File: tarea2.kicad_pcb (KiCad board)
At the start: 2 copper layers, 13 parts, among them IC1 LDO40LPURY, J1 Conn_01x02_Pin, J2 Conn_01x06_Pin, U1 STM32G030K8Tx

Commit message: Colocación inicial de los elementos en la PCB
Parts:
- moved J2 32.3 mm to (146.9, 123.8), turned to 180 degrees
- moved C4(des)2 23.8 mm to (139.3, 104.5), turned to 90 degrees
- moved C4(des)3 23.8 mm to (147.8, 104.5)
- moved IC1 23.8 mm to (143.7, 104.5)
- moved C4(des)1 19.7 mm to (163.0, 111.7)
- moved R1 16.9 mm to (152.0, 116.6), turned to 180 degrees
- moved J1 16.5 mm to (156.0, 104.4), turned to 90 degrees
- moved C1 15.7 mm to (152.0, 119.1), turned to 180 degrees
- moved U1 15.3 mm to (161.5, 119.1), turned to -90 degrees
- moved R2 10.3 mm to (155.6, 112.1), turned to 180 degrees
- moved R3 5.59 mm to (159.9, 112.1)
- moved C3 4.54 mm to (160.0, 108.6), turned to 0 degrees
- moved C2 3.47 mm to (155.6, 108.6), turned to 180 degrees
- renumbered C4(desacople)1 to C4(des)1, C4(desacople)2 to C4(des)2, C4(desacople)3 to C4(des)3
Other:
- board outline added: 37 x 30.5 mm

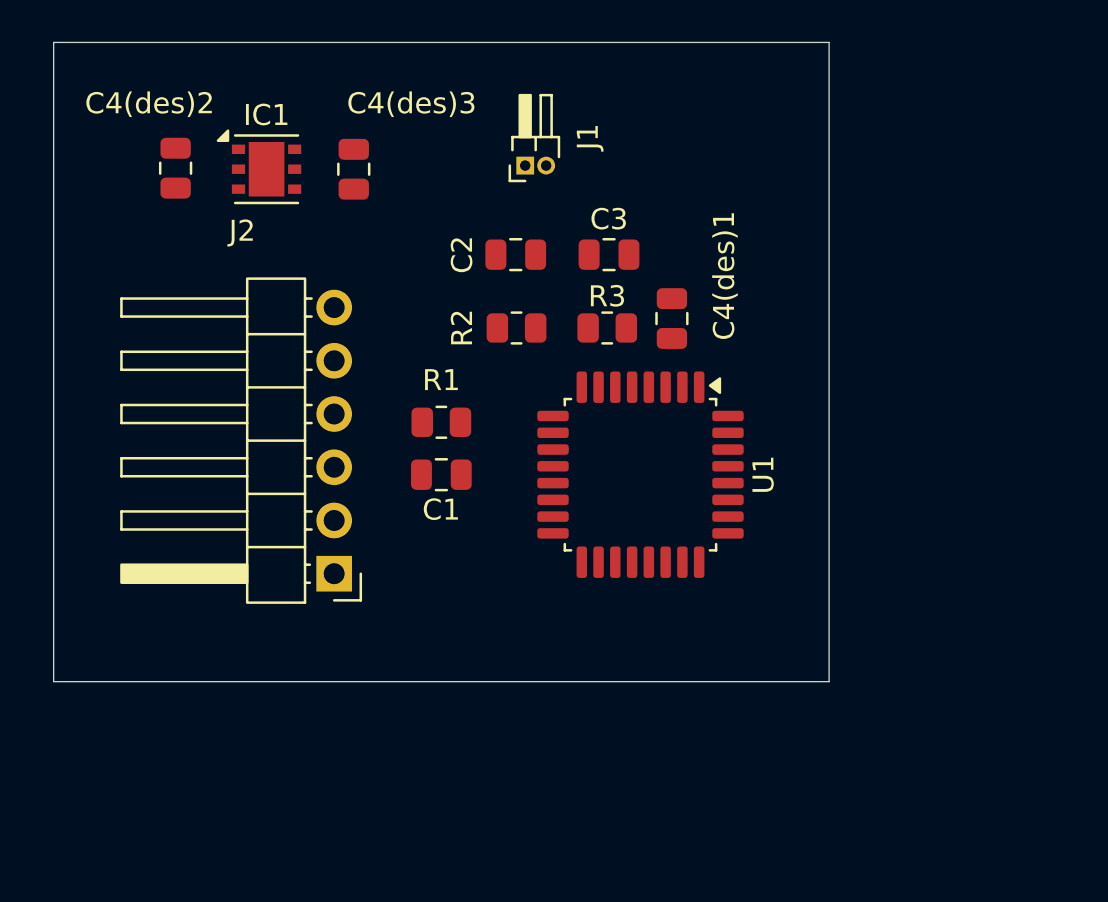
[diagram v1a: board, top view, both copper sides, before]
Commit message: He enrutado los componentes, creando una capa inferior de masa común con vías que facilita el enrutado. He rebajado el margen de holgura a 0,15mm y el DRC está limpio de errores.
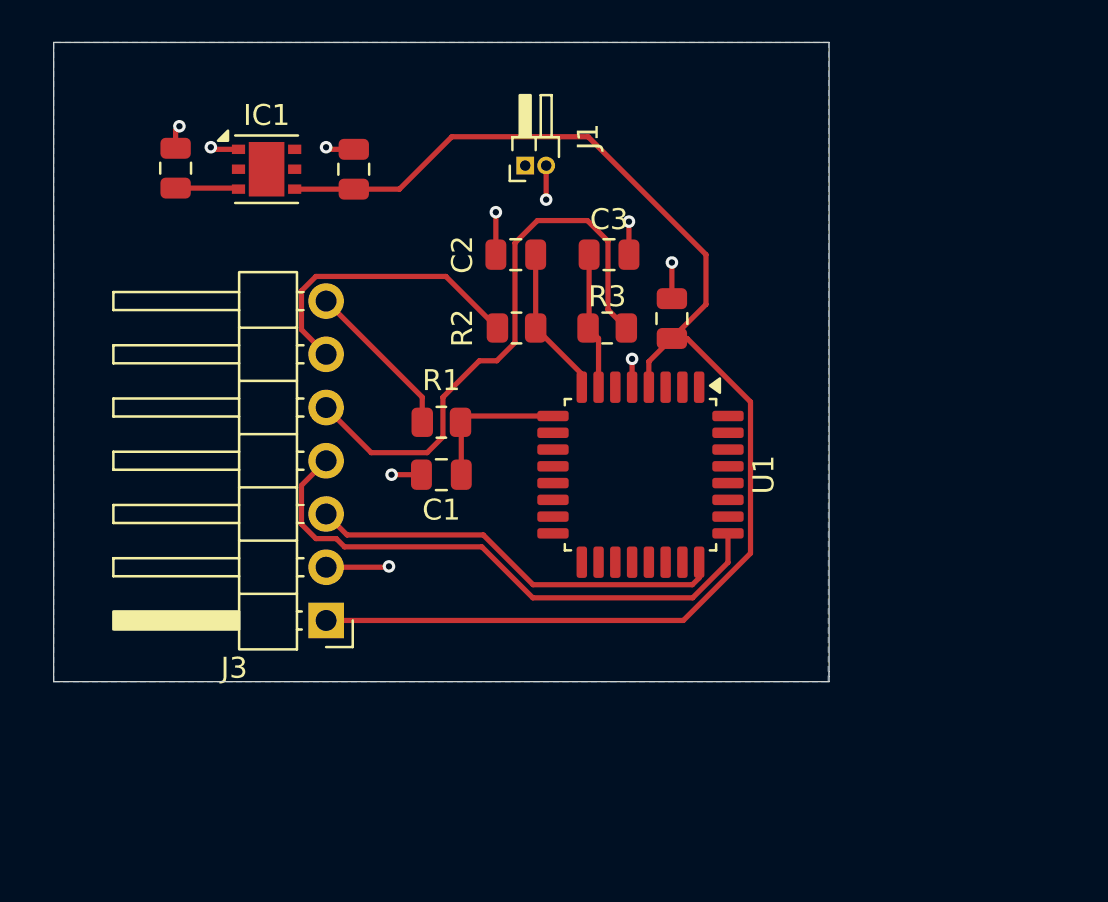
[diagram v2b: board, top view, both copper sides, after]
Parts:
- removed J2: Conn_01x06_Pin, Connector_PinHeader_2.54mm:PinHeader_1x06_P2.54mm_Horizontal
- added J3: Conn_01x07, Connector_PinHeader_2.54mm:PinHeader_1x07_P2.54mm_Horizontal, F.Cu at (146.5, 126.1)
- renumbered C4(des)1 to C4(desacople)1, C4(des)2 to C4(desacople)2, C4(des)3 to C4(desacople)3
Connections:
- C4(desacople)2 pad 2: Net-(IC1-GND_1) -> /Alimentación/GND
- C4(desacople)3 pad 2: Net-(IC1-GND_1) -> /Alimentación/GND
- IC1 pad 1: Net-(IC1-GND_1) -> /Alimentación/GND
- R1 pad 2: unconnected-(R1-Pad2) -> Net-(J3-Pin_7)
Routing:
- net /Alimentación/VDD: track 0.00 -> 64.3 mm
- net Net-(J3-Pin_5): track 0.00 -> 27.7 mm
- net Net-(J3-Pin_4): track 0.00 -> 27.4 mm
- net Net-(J3-Pin_3): track 0.00 -> 20.1 mm
- net /Alimentación/GND: track 0.00 -> 17.2 mm, vias 0 -> 10
- net Net-(J3-Pin_6): track 0.00 -> 14.2 mm
- net Net-(J3-Pin_7): track 0.00 -> 7.69 mm
- net Net-(U1-PA1): track 0.00 -> 7.24 mm
- net Net-(U1-PA2): track 0.00 -> 7.05 mm
- net Net-(U1-PA0): track 0.00 -> 6.55 mm
- net Net-(IC1-VIN): track 0.00 -> 3.02 mm
- added copper zone on B.Cu, net /Alimentación/GND

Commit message: elimada una vía innecesaria
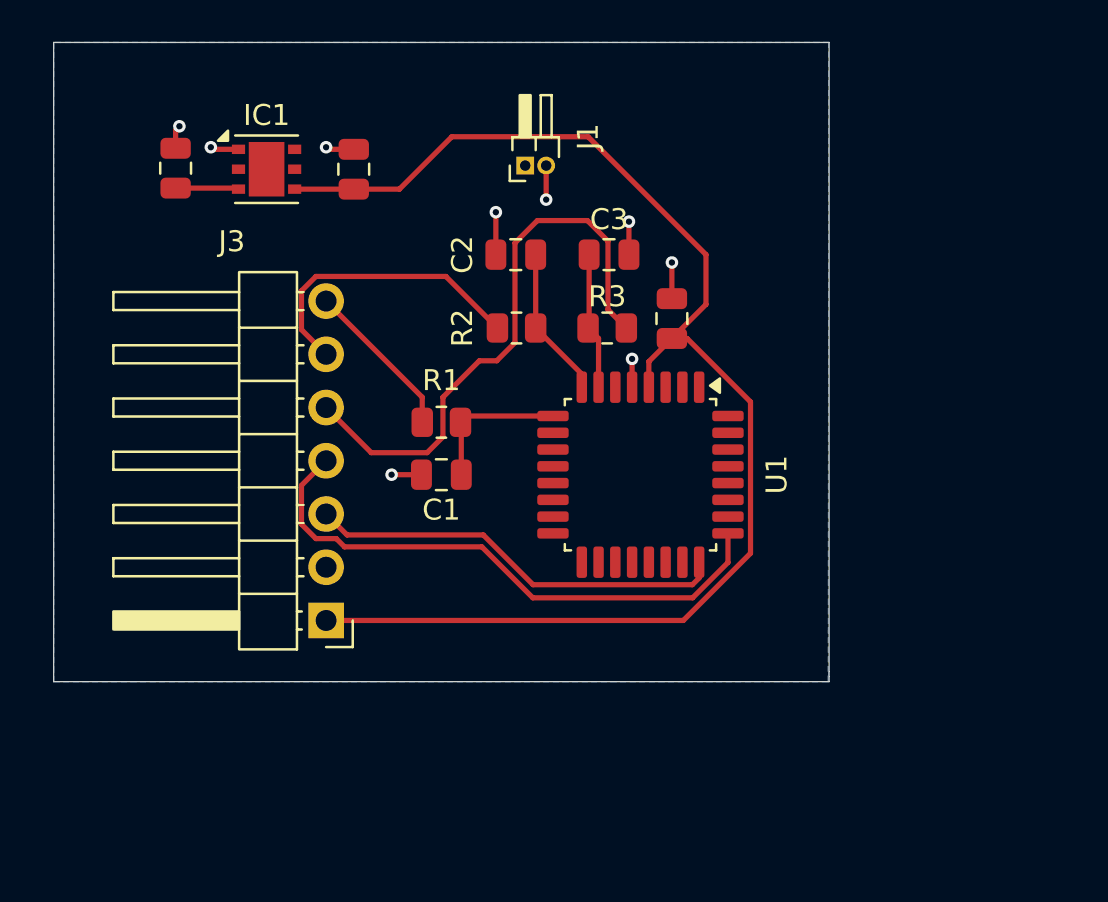
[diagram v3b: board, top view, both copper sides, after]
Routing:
- net /Alimentación/GND: track 17.2 -> 14.2 mm, vias 10 -> 9
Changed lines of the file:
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@@
 		(tags "LQFP QFP")
 		(property "Reference" "U1"
-			(at 0 -5.88 90)
+			(at 0 -6.5 90)
 			(layer "F.SilkS")
 			(effects
@@
 			(layer "F.Fab")
 		)
-		(fp_text user "${REFERENCE}"
-			(at 0 0 90)
-			(layer "F.Fab")
-			(effects
-				(font
-					(size 0.5 0.5)
-					(thickness 0.08)
-				)
-			)
-		)
 		(pad "1" smd roundrect
 			(at -0.95 0 90)
@@
 			(layer "F.Fab")
 		)
-		(fp_text user "${REFERENCE}"
-			(at 0 0 90)
-			(layer "F.Fab")
-			(effects
-				(font
-					(size 0.5 0.5)
-					(thickness 0.08)
-				)
-			)
-		)
 		(pad "1" smd roundrect
 			(at -0.95 0 90)
@@
 		(tags "Through hole angled pin header THT 1x07 2.54mm single row")
 		(property "Reference" "J3"
-			(at 4.385 -2.27 0)
+			(at 4.5 18.08 0)
 			(layer "F.SilkS")
 			(effects
@@
 			(at 4.385 17.51 0)
 			(layer "F.Fab")
+			(hide yes)
 			(effects
 				(font
@@
 			(at 0.425 3.866 0)
 			(layer "F.Fab")
+			(hide yes)
 			(effects
 				(font
@@
 			(layer "F.Fab")
 		)
-		(fp_text user "${REFERENCE}"
-			(at 0 0 90)
-			(layer "F.Fab")
-			(effects
-				(font
-					(size 0.5 0.5)
-					(thickness 0.08)
-				)
-			)
-		)
 		(pad "1" smd roundrect
 			(at -0.95 0 90)
@@
 	)
 	(segment
+		(start 146.013299 109.665)
+		(end 152.215 109.665)
+		(width 0.25)
+		(layer "F.Cu")
+		(net "Net-(J3-Pin_6)")
+	)
+	(segment
+		(start 146.5 113.38)
+		(end 145.325 112.205)
+		(width 0.25)
+		(layer "F.Cu")
+		(net "Net-(J3-Pin_6)")
+	)
+	(segment
+		(start 152.215 109.665)
+		(end 154.675 112.125)
+		(width 0.25)
+		(layer "F.Cu")
+		(net "Net-(J3-Pin_6)")
+	)
+	(segment
+		(start 145.325 112.205)
+		(end 145.325 110.353299)
+		(width 0.25)
+		(layer "F.Cu")
+		(net "Net-(J3-Pin_6)")
+	)
+	(segment
+		(start 145.325 110.353299)
+		(end 146.013299 109.665)
+		(width 0.25)
+		(layer "F.Cu")
+		(net "Net-(J3-Pin_6)")
+	)
+	(segment
 		(start 152.5 103)
 		(end 150 105.5)
@@
 	)
 	(segment
-		(start 146.5 123.54)
-		(end 149.46 123.54)
-		(width 0.25)
-		(layer "F.Cu")
-		(net "/Alimentación/GND")
-	)
-	(segment
 		(start 163 110.725)
 		(end 163 109)
@@
 	)
 	(segment
-		(start 149.46 123.54)
-		(end 149.5 123.5)
-		(width 0.25)
-		(layer "F.Cu")
-		(net "/Alimentación/GND")
-	)
-	(segment
 		(start 139.32 102.68)
 		(end 139.5 102.5)
@@
 	)
 	(via
-		(at 149.5 123.5)
-		(size 0.6)
-		(drill 0.3)
-		(layers "F.Cu" "B.Cu")
-		(net "/Alimentación/GND")
-	)
-	(via
 		(at 154.6 106.6)
 		(size 0.6)
@@
 	)
 	(segment
-		(start 139.32 105.45)
-		(end 142.27 105.45)
-		(width 0.25)
-		(layer "F.Cu")
-		(net "Net-(IC1-VIN)")
-	)
-	(segment
-		(start 142.27 105.45)
-		(end 142.32 105.5)
-		(width 0.25)
-		(layer "F.Cu")
-		(net "Net-(IC1-VIN)")
-	)
-	(segment
 		(start 156.375 124.375)
 		(end 154 122)
@@
 	)
 	(segment
-		(start 155.5125 108.0674)
-		(end 156.5799 107)
+		(start 146.5 118.46)
+		(end 145.325 119.635)
 		(width 0.25)
 		(layer "F.Cu")
-		(net "Net-(J3-Pin_5)")
+		(net "Net-(J3-Pin_4)")
 	)
 	(segment
-		(start 156.5799 107)
-		(end 158.9701 107)
+		(start 146.986701 122.175)
+		(end 147.379899 122.568198)
 		(width 0.25)
 		(layer "F.Cu")
-		(net "Net-(J3-Pin_5)")
+		(net "Net-(J3-Pin_4)")
 	)
 	(segment
-		(start 158.9701 107)
-		(end 159.95 107.9799)
+		(start 165.675 123.31486)
+		(end 165.675 121.925)
 		(width 0.25)
 		(layer "F.Cu")
-		(net "Net-(J3-Pin_5)")
+		(net "Net-(J3-Pin_4)")
 	)
 	(segment
-		(start 146.5 115.92)
-		(end 148.655 118.075)
+		(start 145.325 121.486701)
+		(end 146.013299 122.175)
 		(width 0.25)
 		(layer "F.Cu")
-		(net "Net-(J3-Pin_5)")
+		(net "Net-(J3-Pin_4)")
 	)
 	(segment
-		(start 159.95 111.25)
-		(end 160.825 112.125)
+		(start 145.325 119.635)
+		(end 145.325 121.486701)
 		(width 0.25)
 		(layer "F.Cu")
-		(net "Net-(J3-Pin_5)")
+		(net "Net-(J3-Pin_4)")
 	)
 	(segment
-		(start 148.655 118.075)
-		(end 151.3201 118.075)
+		(start 156.363604 125)
+		(end 163.98986 125)
 		(width 0.25)
 		(layer "F.Cu")
-		(net "Net-(J3-Pin_5)")
+		(net "Net-(J3-Pin_4)")
 	)
 	(segment
-		(start 152.075 115.42745)
-		(end 153.81245 113.69)
+		(start 147.379899 122.568198)
+		(end 153.931802 122.568198)
 		(width 0.25)
 		(layer "F.Cu")
-		(net "Net-(J3-Pin_5)")
+		(net "Net-(J3-Pin_4)")
 	)
 	(segment
-		(start 151.3201 118.075)
-		(end 152.075 117.3201)
+		(start 146.013299 122.175)
+		(end 146.986701 122.175)
 		(width 0.25)
 		(layer "F.Cu")
-		(net "Net-(J3-Pin_5)")
+		(net "Net-(J3-Pin_4)")
 	)
 	(segment
-		(start 153.81245 113.69)
-		(end 154.6426 113.69)
+		(start 153.931802 122.568198)
+		(end 156.363604 125)
 		(width 0.25)
 		(layer "F.Cu")
-		(net "Net-(J3-Pin_5)")
+		(net "Net-(J3-Pin_4)")
 	)
 	(segment
-		(start 159.95 107.9799)
-		(end 159.95 111.25)
+		(start 163.98986 125)
+		(end 165.675 123.31486)
 		(width 0.25)
 		(layer "F.Cu")
-		(net "Net-(J3-Pin_5)")
+		(net "Net-(J3-Pin_4)")
 	)
 	(segment
-		(start 152.075 117.3201)
-		(end 152.075 115.42745)
+		(start 139.32 105.45)
+		(end 142.27 105.45)
 		(width 0.25)
 		(layer "F.Cu")
-		(net "Net-(J3-Pin_5)")
+		(net "Net-(IC1-VIN)")
 	)
 	(segment
-		(start 155.5125 112.8201)
-		(end 155.5125 108.0674)
+		(start 142.27 105.45)
+		(end 142.32 105.5)
 		(width 0.25)
 		(layer "F.Cu")
-		(net "Net-(J3-Pin_5)")
+		(net "Net-(IC1-VIN)")
 	)
 	(segment
-		(start 154.6426 113.69)
-		(end 155.5125 112.8201)
+		(start 155.5125 108.0674)
+		(end 156.5799 107)
 		(width 0.25)
 		(layer "F.Cu")
@@
 	)
 	(segment
-		(start 151.0875 115.4275)
-		(end 151.0875 116.625)
-		(width 0.25)
-		(layer "F.Cu")
-		(net "Net-(J3-Pin_7)")
-	)
-	(segment
-		(start 146.5 110.84)
-		(end 151.0875 115.4275)
-		(width 0.25)
-		(layer "F.Cu")
-		(net "Net-(J3-Pin_7)")
-	)
-	(segment
-		(start 146.5 118.46)
-		(end 145.325 119.635)
-		(width 0.25)
-		(layer "F.Cu")
-		(net "Net-(J3-Pin_4)")
-	)
-	(segment
-		(start 146.986701 122.175)
-		(end 147.379899 122.568198)
+		(start 156.5799 107)
+		(end 158.9701 107)
 		(width 0.25)
 		(layer "F.Cu")
-		(net "Net-(J3-Pin_4)")
+		(net "Net-(J3-Pin_5)")
 	)
 	(segment
-		(start 165.675 123.31486)
-		(end 165.675 121.925)
+		(start 158.9701 107)
+		(end 159.95 107.9799)
 		(width 0.25)
 		(layer "F.Cu")
-		(net "Net-(J3-Pin_4)")
+		(net "Net-(J3-Pin_5)")
 	)
 	(segment
-		(start 145.325 121.486701)
-		(end 146.013299 122.175)
+		(start 146.5 115.92)
+		(end 148.655 118.075)
 		(width 0.25)
 		(layer "F.Cu")
-		(net "Net-(J3-Pin_4)")
+		(net "Net-(J3-Pin_5)")
 	)
 	(segment
-		(start 145.325 119.635)
-		(end 145.325 121.486701)
+		(start 159.95 111.25)
+		(end 160.825 112.125)
 		(width 0.25)
 		(layer "F.Cu")
-		(net "Net-(J3-Pin_4)")
+		(net "Net-(J3-Pin_5)")
 	)
 	(segment
-		(start 156.363604 125)
-		(end 163.98986 125)
+		(start 148.655 118.075)
+		(end 151.3201 118.075)
 		(width 0.25)
 		(layer "F.Cu")
-		(net "Net-(J3-Pin_4)")
+		(net "Net-(J3-Pin_5)")
 	)
 	(segment
-		(start 147.379899 122.568198)
-		(end 153.931802 122.568198)
+		(start 152.075 115.42745)
+		(end 153.81245 113.69)
 		(width 0.25)
 		(layer "F.Cu")
-		(net "Net-(J3-Pin_4)")
+		(net "Net-(J3-Pin_5)")
 	)
 	(segment
-		(start 146.013299 122.175)
-		(end 146.986701 122.175)
+		(start 151.3201 118.075)
+		(end 152.075 117.3201)
 		(width 0.25)
 		(layer "F.Cu")
-		(net "Net-(J3-Pin_4)")
+		(net "Net-(J3-Pin_5)")
 	)
 	(segment
-		(start 153.931802 122.568198)
-		(end 156.363604 125)
+		(start 153.81245 113.69)
+		(end 154.6426 113.69)
 		(width 0.25)
 		(layer "F.Cu")
-		(net "Net-(J3-Pin_4)")
+		(net "Net-(J3-Pin_5)")
 	)
 	(segment
-		(start 163.98986 125)
-		(end 165.675 123.31486)
+		(start 159.95 107.9799)
+		(end 159.95 111.25)
 		(width 0.25)
 		(layer "F.Cu")
-		(net "Net-(J3-Pin_4)")
+		(net "Net-(J3-Pin_5)")
 	)
 	(segment
-		(start 146.013299 109.665)
-		(end 152.215 109.665)
+		(start 152.075 117.3201)
+		(end 152.075 115.42745)
 		(width 0.25)
 		(layer "F.Cu")
-		(net "Net-(J3-Pin_6)")
+		(net "Net-(J3-Pin_5)")
 	)
 	(segment
-		(start 146.5 113.38)
-		(end 145.325 112.205)
+		(start 155.5125 112.8201)
+		(end 155.5125 108.0674)
 		(width 0.25)
 		(layer "F.Cu")
-		(net "Net-(J3-Pin_6)")
+		(net "Net-(J3-Pin_5)")
 	)
 	(segment
-		(start 152.215 109.665)
-		(end 154.675 112.125)
+		(start 154.6426 113.69)
+		(end 155.5125 112.8201)
 		(width 0.25)
 		(layer "F.Cu")
-		(net "Net-(J3-Pin_6)")
+		(net "Net-(J3-Pin_5)")
 	)
 	(segment
-		(start 145.325 112.205)
-		(end 145.325 110.353299)
+		(start 151.0875 115.4275)
+		(end 151.0875 116.625)
 		(width 0.25)
 		(layer "F.Cu")
-		(net "Net-(J3-Pin_6)")
+		(net "Net-(J3-Pin_7)")
 	)
 	(segment
-		(start 145.325 110.353299)
-		(end 146.013299 109.665)
+		(start 146.5 110.84)
+		(end 151.0875 115.4275)
 		(width 0.25)
 		(layer "F.Cu")
-		(net "Net-(J3-Pin_6)")
+		(net "Net-(J3-Pin_7)")
 	)
 	(zone

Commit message: He completado la parte 1 de la práctica 4 y he subsanado los errores de la DRC
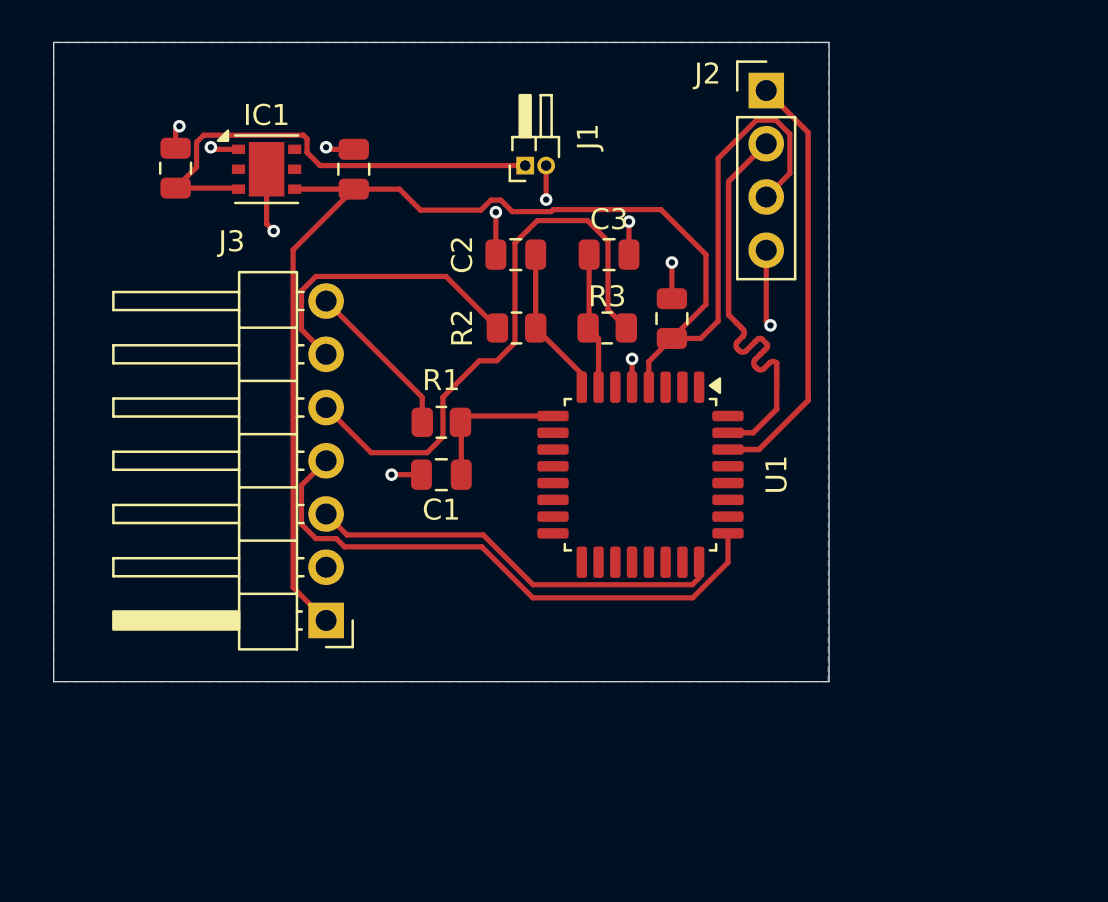
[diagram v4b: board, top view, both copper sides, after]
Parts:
- added J2: BUS I2C, Connector_PinHeader_2.54mm:PinHeader_1x04_P2.54mm_Vertical, F.Cu at (167.5, 100.8)
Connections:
- IC1 pad 7: Net-(IC1-GND_1) -> /Alimentación/GND
- J1 pad 1: unconnected-(J1-Pin_1-Pad1) -> Net-(IC1-VIN)
- U1 pad 30: unconnected-(U1-PB6-Pad30) -> Net-(J2-Pin_1)
- U1 pad 31: unconnected-(U1-PB7-Pad31) -> Net-(J2-Pin_2)
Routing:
- net Net-(J2-Pin_1): track 0.00 -> 20.4 mm
- net Net-(J2-Pin_2): track 0.00 -> 20.3 mm
- net Net-(IC1-VIN): track 3.02 -> 22.4 mm
- net /Alimentación/GND: track 14.2 -> 20.9 mm, vias 9 -> 11
- net /Alimentación/VDD: track 64.3 -> 70.4 mm
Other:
- copper layers 2 -> 4

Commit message: Se han añadido un receptor de USB tipo C, un CH340 y sus respectivos componentes para su correcto funcionamiento para completar la tarea de enrutado diferencial de la Sesion-4
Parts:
- added C4(desacople)4: 100n, Capacitor_SMD:C_0805_2012Metric, F.Cu at (158.5, 127.0)
- added J4: USB_C_Receptacle_USB2.0_16P, Connector_USB:USB_C_Receptacle_GCT_USB4105-xx-A_16P_TopMnt_Horizontal, F.Cu at (166.5, 130.5)
- added R4: 5.1k, Resistor_SMD:R_0805_2012Metric, F.Cu at (154.5, 131.1)
- added R5: 5.1k, Resistor_SMD:R_0805_2012Metric, F.Cu at (154.5, 134.0)
- added U2: CH340N, Package_SO:JEITA_SOIC-8_3.9x4.9mm_P1.27mm, F.Cu at (152.3, 125.2)
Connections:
- U1 pad 22: unconnected-(U1-PA9/PA11-Pad22) -> Net-(U1-PA9/PA11)
- U1 pad 23: unconnected-(U1-PA10/PA12-Pad23) -> Net-(U1-PA10/PA12)
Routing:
- net /Alimentación/VDD: track 70.4 -> 110.8 mm, vias 0 -> 3
- net USB_D-: track 0.00 -> 16.8 mm
- net USB_D+: track 0.00 -> 16.6 mm
- net Net-(U1-PA10/PA12): track 0.00 -> 13.8 mm
- net /Alimentación/GND: track 20.9 -> 33.7 mm, vias 11 -> 17
- net Net-(J4-CC2): track 0.00 -> 12.2 mm, vias 0 -> 2
- net Net-(U1-PA9/PA11): track 0.00 -> 9.20 mm
- net Net-(J4-CC1): track 0.00 -> 8.34 mm
- net Net-(J3-Pin_4): track 27.4 -> 22.6 mm, vias 0 -> 1
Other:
- board size 37 x 30.5 mm -> 37 x 39 mm
